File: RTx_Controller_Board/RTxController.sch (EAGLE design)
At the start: 197 parts, among them IC2 MAX5984C, J22 Debug Header, SW1 COM08720, U1 STM32F407ZXT, U2 TPD4S012, U3 KSZ8081, X4 MINI-USB-32005-301, X8 0826-1X1T-GJ-F

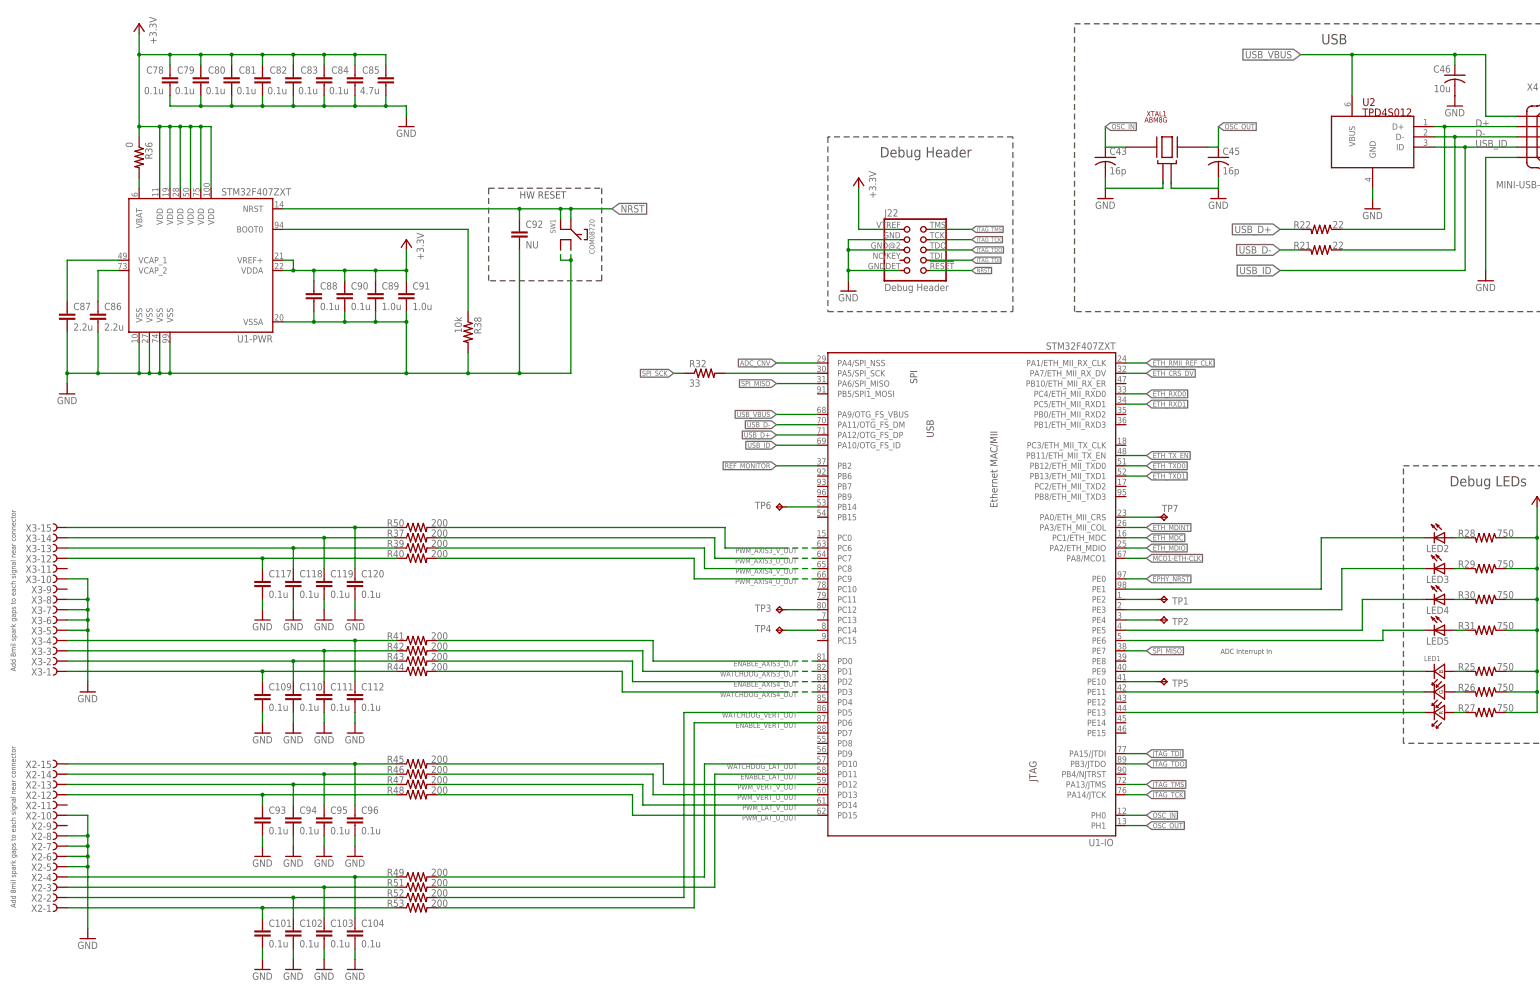
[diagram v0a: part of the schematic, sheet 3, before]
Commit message: Rtx Controller board updated, all that remains are power planes and rework by Rob. Initial check in of crystal.lbr.
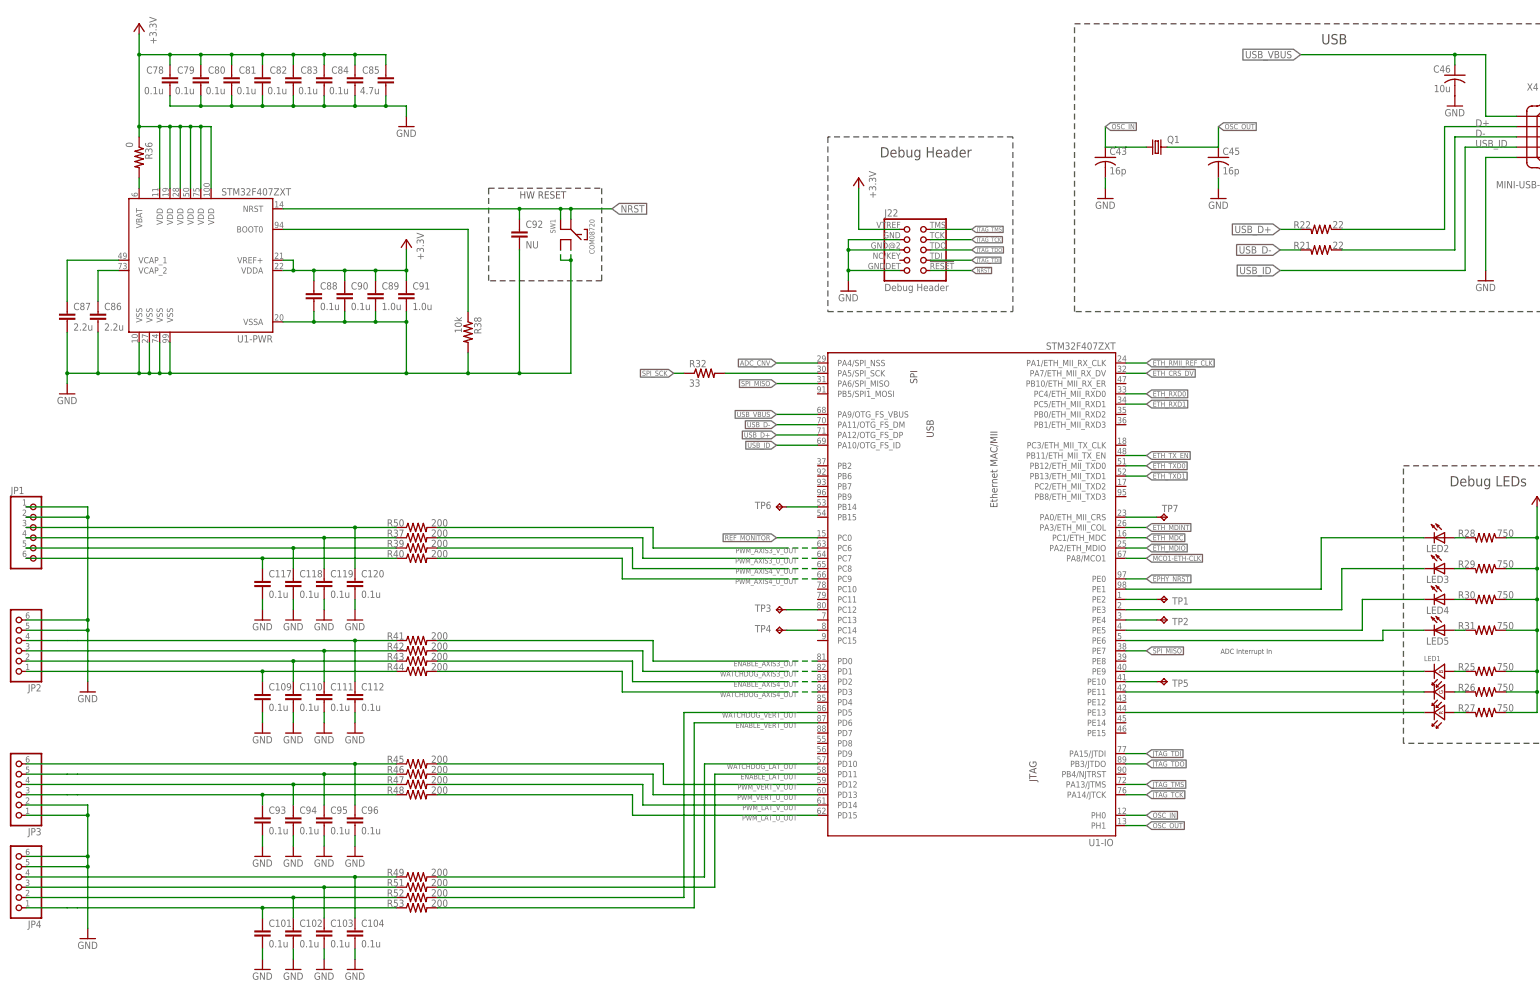
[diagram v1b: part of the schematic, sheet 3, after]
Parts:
- removed U2: TPD4S012, rtx:TPD4S012
- removed X1, X2, X3: (no value), con-subd:F15HDHS
- removed XTAL1: ABM8G, motorFeedback:ABM8G
- added JP1, JP2, JP3, JP4, JP5, JP6: (no value), pinhead:PINHD-1X6
- added Q1: (no value), crystal:CRYSTALCTS406
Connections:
- removed net SPI_NSS: ADC1.CNV@6, ADC1.SDI@9, ADC2.CNV@6, ADC3.CNV@6, ADC4.CNV@6
- net +5.000VREF: now also JP5.5, JP5.6, JP6.5, JP6.6; no longer X1-10.F, X1-13.F, X1-14.F, X1-9.F
- net ADC_CNV: now also ADC1.CNV@6, ADC1.SDI@9, ADC2.CNV@6, ADC3.CNV@6, ADC4.CNV@6
- net D+: no longer U2.D+
- net D-: no longer U2.D-
- net GND: now also JP1.1, JP1.2, JP2.5, JP2.6, JP3.1, JP3.2, JP4.5, JP4.6, JP5.1, JP5.2, JP6.1, JP6.2; no longer U2.GND, X1-5.F, X1-6.F, X1-7.F, X1-8.F, X2-10.F, X2-5.F, X2-6.F, X2-7.F, X2-8.F, X3-10.F, X3-5.F, X3-6.F, X3-7.F, X3-8.F
- net N$14: now also JP6.4; no longer X1-2.F
- net N$42: now also JP3.6; no longer X2-15.F
- net N$45: now also JP3.5; no longer X2-14.F
- net N$46: now also JP3.4; no longer X2-13.F
- net N$47: now also JP3.3; no longer X2-12.F
- net N$48: now also JP4.4; no longer X2-4.F
- net N$49: now also JP4.3; no longer X2-3.F
- net N$50: now also JP4.2; no longer X2-2.F
- net N$51: now also JP4.1; no longer X2-1.F
- net N$52: now also JP2.4; no longer X3-4.F
- net N$53: now also JP2.3; no longer X3-3.F
- net N$54: now also JP2.2; no longer X3-2.F
- net N$55: now also JP2.1; no longer X3-1.F
- net N$6: now also JP5.4; no longer X1-4.F
- net N$61: now also JP1.3; no longer X3-15.F
- net N$62: now also JP1.4; no longer X3-14.F
- net N$63: now also JP1.5; no longer X3-13.F
- net N$64: now also JP1.6; no longer X3-12.F
- net N$7: now also JP6.3; no longer X1-1.F
- net N$9: now also JP5.3; no longer X1-3.F
- net OSC_IN: now also Q1.1; no longer XTAL1.1
- net OSC_OUT: now also Q1.2; no longer XTAL1.3
- net REF_MONITOR: now also U1-IO.PC0@15; no longer U1-IO.PB2@37
- net USB_ID: no longer U2.ID
- net USB_VBUS: no longer U2.VBUS
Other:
- note removed: "Add 8mil spark gaps to each signal near connector"

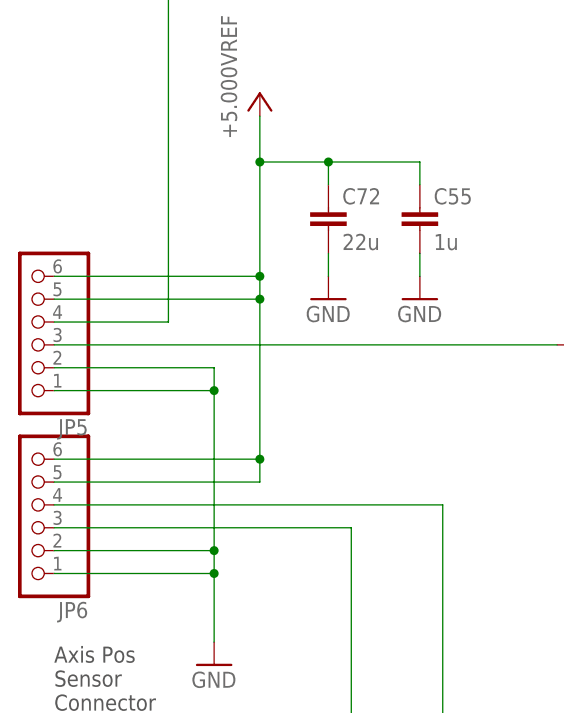
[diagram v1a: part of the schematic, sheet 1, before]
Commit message: Repositioned LDO's created power planes.
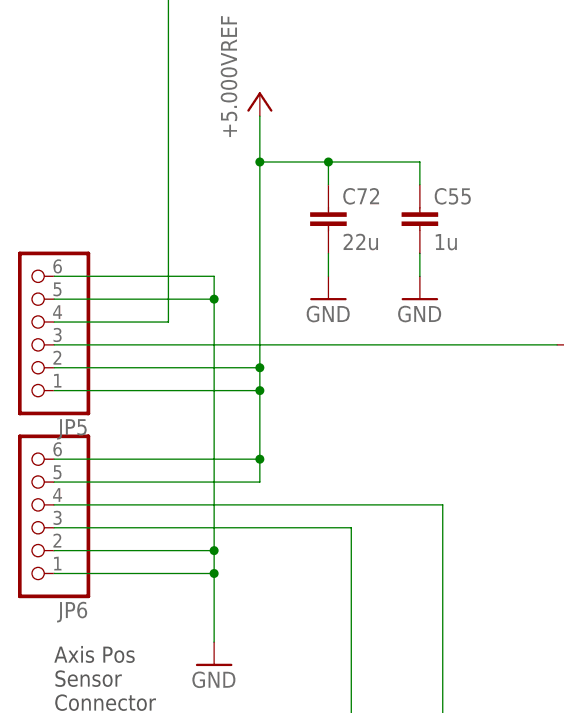
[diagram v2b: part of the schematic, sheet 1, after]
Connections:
- removed net VIO: ADC1.VIO@10, ADC2.VIO@10, ADC3.VIO@10, C5.1, C7.1, C9.1
- removed net VIO@10: ADC4.VIO@10, C42.1
- net +3.3V: now also ADC1.VIO@10, ADC2.VIO@10, ADC3.VIO@10, ADC4.VIO@10, C42.1, C5.1, C7.1, C9.1
- net +5.000VREF: now also JP5.1, JP5.2; no longer JP5.5, JP5.6
- net GND: now also JP5.5, JP5.6; no longer JP5.1, JP5.2

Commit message: High speed signal routing information added to schematic. Updated Precharge board.
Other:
- note added: "(NC)"
- note added: "-Route D+/D- traces parallel and within 2 mils of each other -D+/D- traces should not have any extra components to maintain signal integrity. -0.3048 mm traces"
- note added: "0.5mm trace"
- note added: "Rx+/Rx- routed together Seperation < 0.25mm 0.25mm traces"
- note added: "Seperation of Tx/Rx differential pairs > 0.5mm"
- note added: "Tx+/Tx- routed together Seperation < 0.25mm 0.25mm traces"
- note removed: "High Speed Signal Routing -------------------------------- The Tx+/Tx- and Rx+/Rx- traces should always be as short as possible (less than 25 mm or 1"). If longer traces are absolutely required, the maximum length is limited to 75 mm (3"). The individual trace impedance of Tx+/Tx- and Rx+/Rx- must be kept below 50 ohms, and the differential characteristic impedance of the pair must be 100 ohms. R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"
- moved on the sheet: C43, C44, C45, C48, C50, C51, C54, C73, C75, C76, C77, C97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

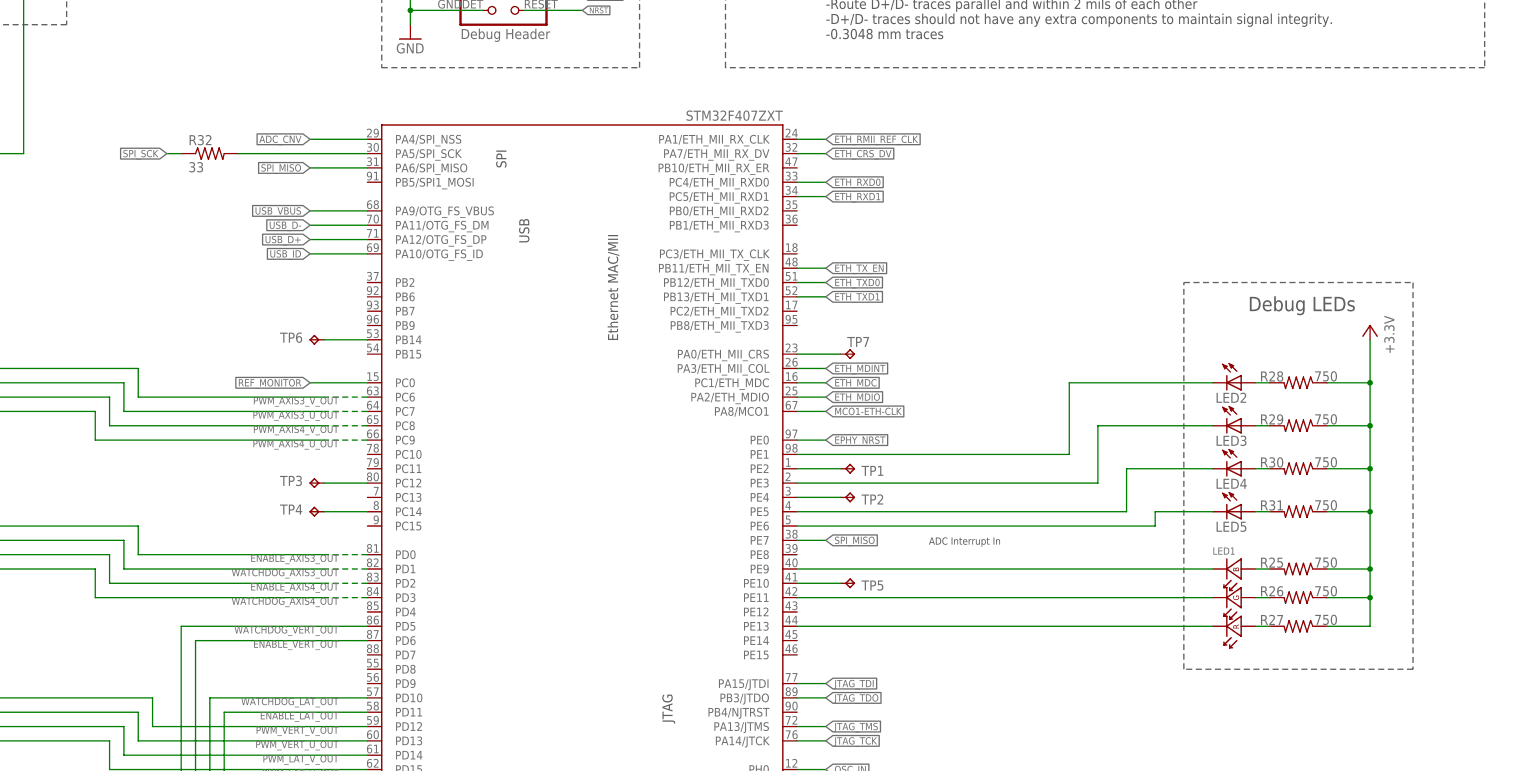
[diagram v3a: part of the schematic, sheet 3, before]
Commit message: Added termination resistors to RMII bus, adjusted width of digital signals.
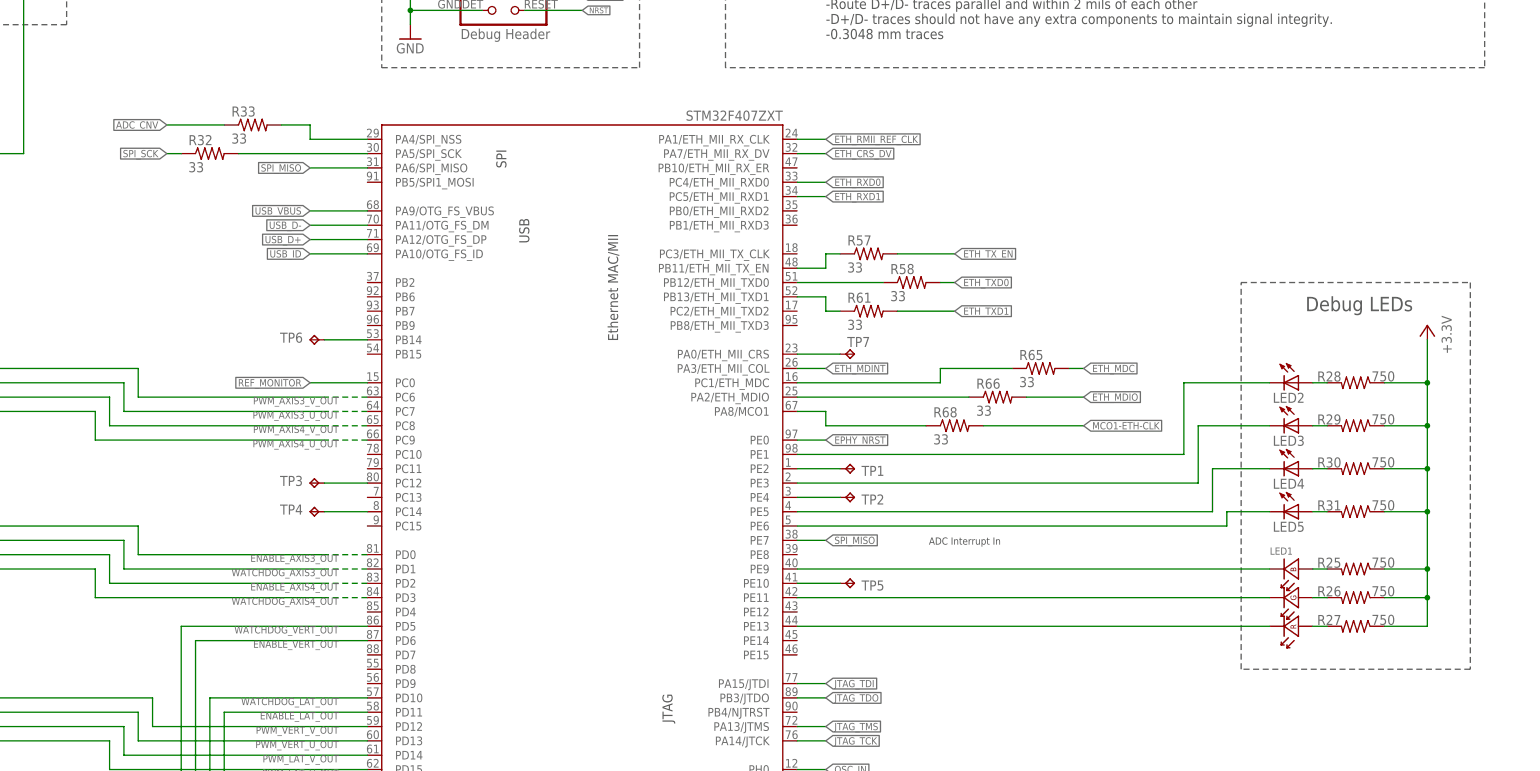
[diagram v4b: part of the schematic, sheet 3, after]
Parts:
- added R33, R57, R58, R61, R65, R66, R68: 33, motorFeedback:R-US_R0402
- added R34, R35, R62, R63, R64, R67: 33, rcl_custom:R-US_0402-C-NOSILK
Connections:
- net N$72 renamed SPI_SCK_MCU
- new net N$72: R35.1, U3.RXD0
- new net N$73: R33.2, U1-IO.PA4/SPI_NSS@29
- new net N$74: R34.1, U3.RXD1
- new net N$75: R57.1, U1-IO.PB11/ETH_MII_TX_EN@48
- new net N$76: R61.1, U1-IO.PB13/ETH_MII_TXD1@52
- new net N$77: R58.1, U1-IO.PB12/ETH_MII_TXD0@51
- new net N$78: R62.1, U3.REF_CLK
- new net N$81: R65.1, U1-IO.PC1/ETH_MDC@16
- new net N$83: R63.1, U3.INTRP
- new net N$84: R64.1, U3.CRS_DV/PHYADD
- new net N$85: R66.1, U1-IO.PA2/ETH_MDIO@25
- new net N$86: R68.1, U1-IO.PA8/MCO1@67
- new net N$87: R67.1, U3.MDIO
- net ADC_CNV: now also R33.1; no longer U1-IO.PA4/SPI_NSS@29
- net ETH_CRS_DV: now also R64.2; no longer U3.CRS_DV/PHYADD
- net ETH_MDC: now also R65.2; no longer U1-IO.PC1/ETH_MDC@16
- net ETH_MDINT: now also R63.2; no longer U3.INTRP
- net ETH_MDIO: now also R66.2, R67.2; no longer U1-IO.PA2/ETH_MDIO@25, U3.MDIO
- net ETH_RMII_REF_CLK: now also R62.2; no longer U3.REF_CLK
- net ETH_RXD0: now also R35.2; no longer U3.RXD0
- net ETH_RXD1: now also R34.2; no longer U3.RXD1
- net ETH_TXD0: now also R58.2; no longer U1-IO.PB12/ETH_MII_TXD0@51
- net ETH_TXD1: now also R61.2; no longer U1-IO.PB13/ETH_MII_TXD1@52
- net ETH_TX_EN: now also R57.2; no longer U1-IO.PB11/ETH_MII_TX_EN@48
- net MCO1-ETH-CLK: now also R68.2; no longer U1-IO.PA8/MCO1@67
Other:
- moved on the sheet: LED2, LED3, LED4, LED5, R25, R26, R27, R28, R29, R30, R31, R55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

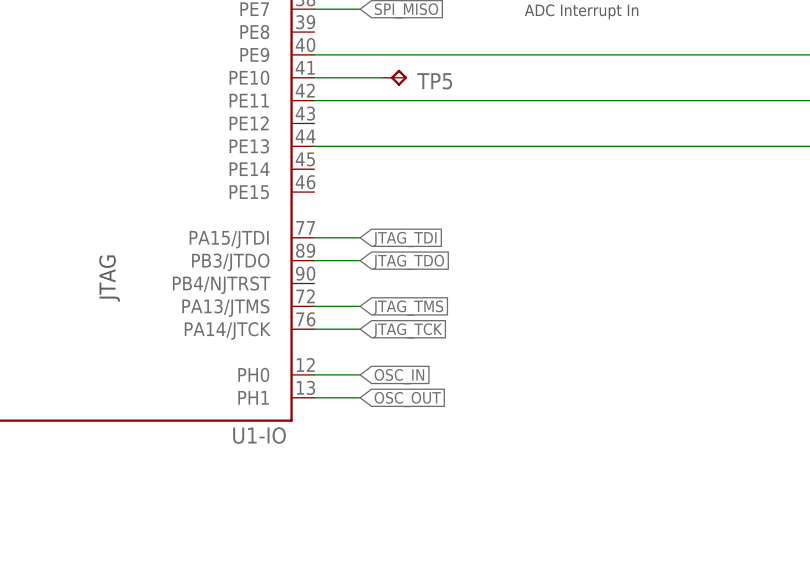
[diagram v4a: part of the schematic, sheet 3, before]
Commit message: Reduced board width.
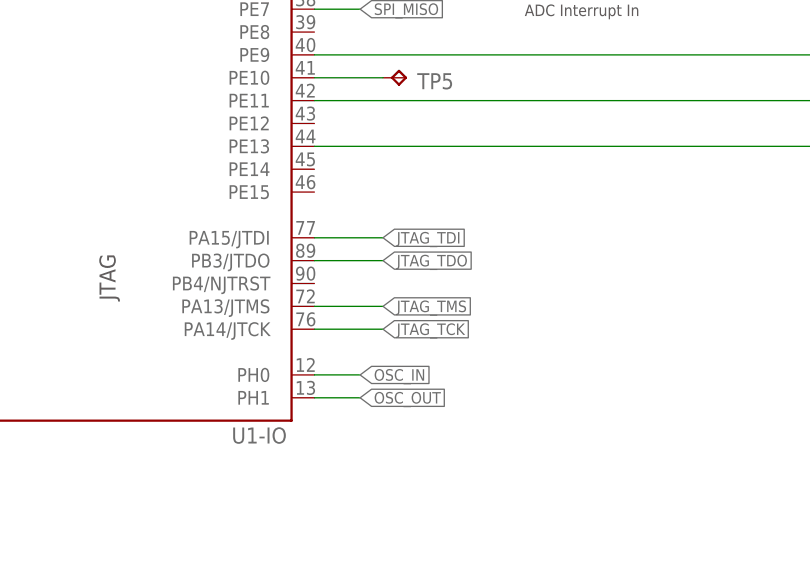
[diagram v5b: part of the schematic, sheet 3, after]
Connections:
- net JTAG_TCK: now also U1-IO.PA14/JTCK@76
- net JTAG_TDI: now also U1-IO.PA15/JTDI@77
- net JTAG_TDO: now also U1-IO.PB3/JTDO@89
- net JTAG_TMS: now also U1-IO.PA13/JTMS@72
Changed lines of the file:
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@@
 </segment>
 <segment>
-<wire x1="284.48" y1="55.88" x2="289.56" y2="55.88" width="0.1524" layer="91"/>
-<label x="289.56" y="55.88" size="1.27" layer="95" xref="yes"/>
+<wire x1="284.48" y1="55.88" x2="292.1" y2="55.88" width="0.1524" layer="91"/>
+<label x="292.1" y="55.88" size="1.27" layer="95" xref="yes"/>
+<pinref part="U1" gate="-IO" pin="PA13/JTMS@72"/>
 </segment>
 </net>
@@
 </segment>
 <segment>
-<wire x1="284.48" y1="53.34" x2="289.56" y2="53.34" width="0.1524" layer="91"/>
-<label x="289.56" y="53.34" size="1.27" layer="95" xref="yes"/>
+<wire x1="284.48" y1="53.34" x2="292.1" y2="53.34" width="0.1524" layer="91"/>
+<label x="292.1" y="53.34" size="1.27" layer="95" xref="yes"/>
+<pinref part="U1" gate="-IO" pin="PA14/JTCK@76"/>
 </segment>
 </net>
@@
 </segment>
 <segment>
-<wire x1="284.48" y1="63.5" x2="289.56" y2="63.5" width="0.1524" layer="91"/>
-<label x="289.56" y="63.5" size="1.27" layer="95" xref="yes"/>
+<wire x1="284.48" y1="63.5" x2="292.1" y2="63.5" width="0.1524" layer="91"/>
+<label x="292.1" y="63.5" size="1.27" layer="95" xref="yes"/>
+<pinref part="U1" gate="-IO" pin="PA15/JTDI@77"/>
 </segment>
 </net>
@@
 </segment>
 <segment>
-<wire x1="284.48" y1="60.96" x2="289.56" y2="60.96" width="0.1524" layer="91"/>
-<label x="289.56" y="60.96" size="1.27" layer="95" xref="yes"/>
+<wire x1="284.48" y1="60.96" x2="292.1" y2="60.96" width="0.1524" layer="91"/>
+<label x="292.1" y="60.96" size="1.27" layer="95" xref="yes"/>
+<pinref part="U1" gate="-IO" pin="PB3/JTDO@89"/>
 </segment>
 </net>
